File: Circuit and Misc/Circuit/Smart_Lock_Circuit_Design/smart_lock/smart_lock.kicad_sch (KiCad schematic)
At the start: 23 parts

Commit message: schematic development
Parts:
- removed J?: Bluepill header1, symbol Connector:Conn_01x20_Female
- removed J?: Bluepill header2, symbol Connector:Conn_01x20_Female
- added BT?: Battery, symbol Device:Battery
- added J?: RTC, symbol Connector:Conn_01x04_Male
- added R?: R, symbol Device:R
- added U? (x3): LM2596, symbol LM2596_Module:LM2596
- added U?: Bluepill_LDO, symbol Bluepill_LDO:Bluepill_LDO
- added U?: 24LC16, symbol Memory_EEPROM:24LC16
- added U?: STM32F103C8Tx, Package_QFP:LQFP-48_7x7mm_P0.5mm, symbol MCU_ST_STM32F1:STM32F103C8Tx
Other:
- note added: "DEVICES USING I2C COMMUNICATION"
- note added: "DEVICES USING UART COMMUNICATION"
- note added: "DRIVER CIRCUIT FOR BUZZER"
- note added: "DRIVER CIRCUIT FOR LOCK"
- note added: "GPIO INPUT DEVICES"
- note added: "MICROCONTROLLER"
- note added: "POWER SECTION"
- moved on the sheet: BZ?, D?, J?, L?, Q?, R?, SW?, U?A, U?B, U?C

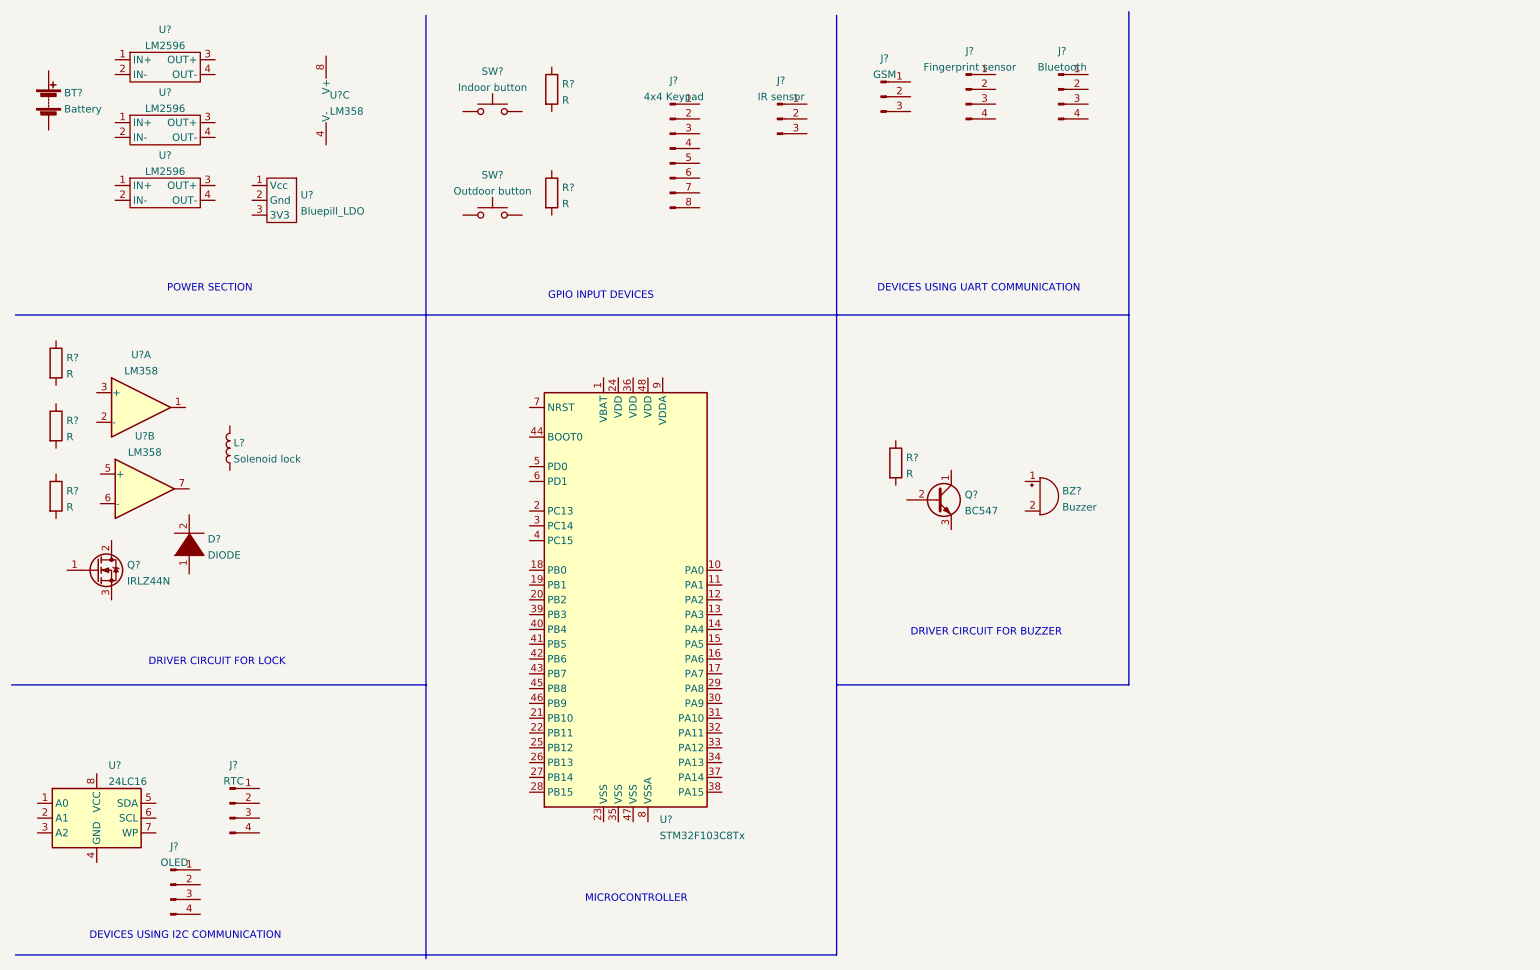
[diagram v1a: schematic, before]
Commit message: schematic update
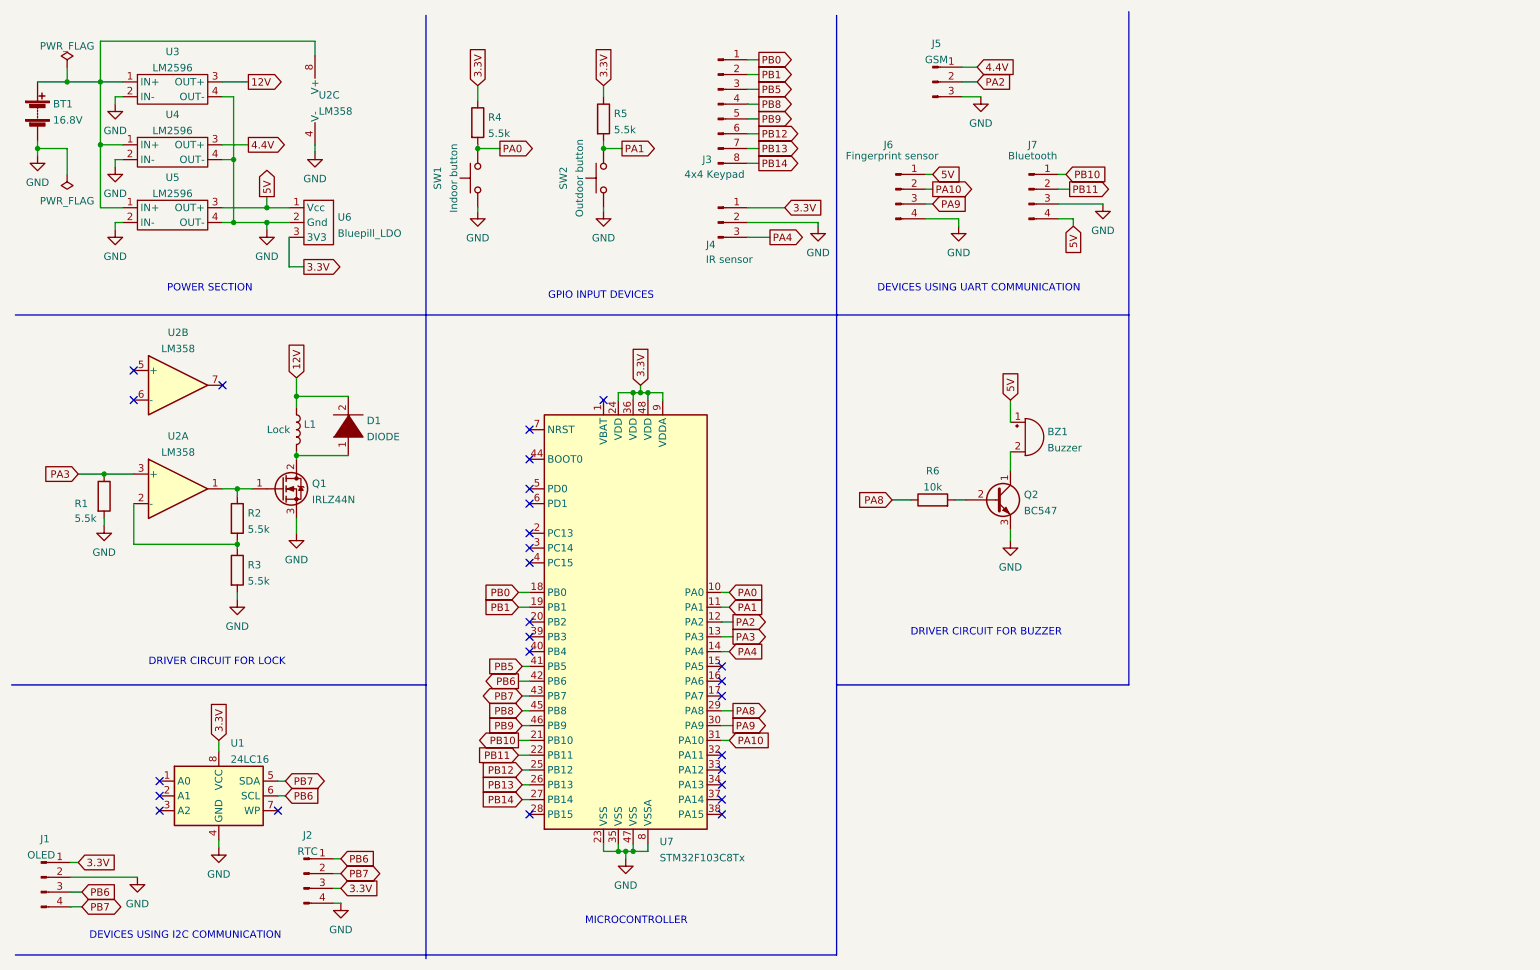
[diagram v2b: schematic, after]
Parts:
- removed U? (x3): LM2596, symbol LM2596_Module:LM2596
- added U3, U4, U5: LM2596, symbol LM2596_Module:LM2596
- BT1: renamed from BT?; value Battery -> 16.8V
- L1: renamed from L?; value Solenoid lock -> Lock
- R1, R2, R3, R4, R5: renamed from R?; value R -> 5.5k
- R6: renamed from R?; value R -> 10k
- gave numbers to parts that had none: 17
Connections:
- net 12V: now reaches L1.1
- net 12V: now also D1.2 (A), U3.3 (OUT+)
- net at L1.2: now also D1.1 (K), Q1.2 (D)
- net GND: now reaches SW1.1 (A), SW1.2 (A)
- net GND: now also BT1.2 (-), J1.2 (Pin_2), J2.4 (Pin_4), J4.2 (Pin_2), J5.3 (Pin_3), J6.4 (Pin_4), J7.3 (Pin_3), Q1.3 (S), Q2.3 (E), R1.2, R3.2, SW2.1 (A), SW2.2 (A), U1.4 (GND), U2.4 (V-), U6.2 (Gnd), U7.23 (VSS), U7.35 (VSS), U7.47 (VSS), U7.8 (VSSA), U3.2 (IN-), U3.4 (OUT-), U4.2 (IN-), U4.4 (OUT-), U5.2 (IN-), U5.4 (OUT-)
- net PA0: now reaches SW1.3 (B), SW1.4 (B)
- net PA0: now also R4.2, U7.10 (PA0)
- net PB6: now reaches J2.1 (Pin_1)
- net PB6: now also J1.3 (Pin_3), U1.6 (SCL), U7.42 (PB6)
- net PB7: now reaches J2.2 (Pin_2)
- net PB7: now also J1.4 (Pin_4), U1.5 (SDA), U7.43 (PB7)
- net 3.3V: now reaches J2.3 (Pin_3)
- net 3.3V: now also J1.1 (Pin_1), J4.1 (Pin_1), R4.1, R5.1, U1.8 (VCC), U6.3 (3V3), U7.24 (VDD), U7.36 (VDD), U7.48 (VDD), U7.9 (VDDA)
- net PB0: now reaches J3.1 (Pin_1)
- net PB0: now also U7.18 (PB0)
- net PB1: now reaches J3.2 (Pin_2)
- net PB1: now also U7.19 (PB1)
- net PB5: now reaches J3.3 (Pin_3)
- net PB5: now also U7.41 (PB5)
- net PB8: now reaches J3.4 (Pin_4)
- net PB8: now also U7.45 (PB8)
- net PB9: now reaches J3.5 (Pin_5)
- net PB9: now also U7.46 (PB9)
- net PB12: now reaches J3.6 (Pin_6)
- net PB12: now also U7.25 (PB12)
- net PB13: now reaches J3.7 (Pin_7)
- net PB13: now also U7.26 (PB13)
- net PB14: now reaches J3.8 (Pin_8)
- net PB14: now also U7.27 (PB14)
- net at U2.1: now also Q1.1 (G), R2.1
- net at U2.2 (-): now also R2.2, R3.1
- net PA3: now reaches U2.3 (+)
- net PA3: now also R1.1, U7.13 (PA3)
- net PA4: now reaches J4.3 (Pin_3)
- net PA4: now also U7.14 (PA4)
- net 5V: now reaches J6.1 (Pin_1)
- net 5V: now also BZ1.1 (-), J7.4 (Pin_4), U6.1 (Vcc), U5.3 (OUT+)
- net PA10: now reaches J6.2 (Pin_2)
- net PA10: now also U7.31 (PA10)
- net PA9: now reaches J6.3 (Pin_3)
- net PA9: now also U7.30 (PA9)
- net PB10: now reaches J7.1 (Pin_1)
- net PB10: now also U7.21 (PB10)
- net PB11: now reaches J7.2 (Pin_2)
- net PB11: now also U7.22 (PB11)
- net at BZ1.2 (+): now also Q2.1 (C)
- net PA8: now reaches R6.1
- net PA8: now also U7.29 (PA8)
- net at R6.2: now also Q2.2 (B)
- net PA1: now reaches SW2.3 (B), SW2.4 (B)
- net PA1: now also R5.2, U7.11 (PA1)
- net 4.4V: now reaches J5.1 (Pin_1)
- net 4.4V: now also U4.3 (OUT+)
- net PA2: now reaches J5.2 (Pin_2)
- net PA2: now also U7.12 (PA2)
- net at BT1.1 (+): now also U2.8 (V+), U3.1 (IN+), U4.1 (IN+), U5.1 (IN+)
- no-connect marks 0 -> 27
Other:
- moved on the sheet: BT1, BZ1, D1, J1, J2, J3, J4, J5, J6, J7, L1, Q1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

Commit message: updated schematic
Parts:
- removed J4: IR sensor, symbol Connector:Conn_01x03_Male
- added J4: Ultrasonic sensor, symbol Connector:Conn_01x04_Male
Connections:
- net 5V: now also J4.1 (Pin_1)
- net GND: now also J4.2 (Pin_2)
- net PA4: now also J4.3 (Pin_3)
- net PA6: now reaches U7.16 (PA6)
- net PA6: now also J4.4 (Pin_4)
- no-connect marks 27 -> 26
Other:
- note added: "Echo"
- note added: "Trig"
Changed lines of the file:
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@@
   (no_connect (at 100.33 118.745))
   (no_connect (at 133.35 128.905))
-  (no_connect (at 133.35 126.365))
   (no_connect (at 133.35 123.825))
   (no_connect (at 100.33 116.205))
@@
     (stroke (width 0) (type default) (color 0 0 0 0))
   )
-  (wire (pts (xy 137.795 45.085) (xy 144.145 45.085))
+  (wire (pts (xy 134.62 49.53) (xy 137.795 49.53))
+    (stroke (width 0) (type default) (color 0 0 0 0))
+  )
+  (wire (pts (xy 134.62 52.07) (xy 149.225 52.07))
     (stroke (width 0) (type default) (color 0 0 0 0))
   )
@@
     (stroke (width 0) (type default) (color 0 0 0 0))
   )
+  (wire (pts (xy 134.62 57.15) (xy 137.795 57.15))
+    (stroke (width 0) (type default) (color 0 0 0 0))
+  )
   (wire (pts (xy 21.59 162.56) (xy 23.495 162.56))
     (stroke (width 0) (type default) (color 0 0 0 0))
@@
     (stroke (width 0) (type default) (color 0 0 0 0))
   )
-  (wire (pts (xy 137.795 47.625) (xy 149.86 47.625))
-    (stroke (width 0) (type default) (color 0 0 0 0))
-  )
   (wire (pts (xy 29.21 47.625) (xy 30.48 47.625))
     (stroke (width 0) (type default) (color 0 0 0 0))
@@
     (stroke (width 0) (type default) (color 0 0 0 0))
   )
-  (wire (pts (xy 149.86 47.625) (xy 149.86 48.26))
+  (wire (pts (xy 149.225 52.07) (xy 149.225 52.705))
     (stroke (width 0) (type default) (color 0 0 0 0))
   )
@@
     (stroke (width 0) (type default) (color 0 0 0 0))
   )
-  (wire (pts (xy 137.795 50.165) (xy 141.605 50.165))
+  (wire (pts (xy 134.62 54.61) (xy 137.16 54.61))
     (stroke (width 0) (type default) (color 0 0 0 0))
   )
@@
     (stroke (width 0) (type default) (color 0 0 0 0))
   )
+  (wire (pts (xy 133.35 126.365) (xy 135.255 126.365))
+    (stroke (width 0) (type default) (color 0 0 0 0))
+  )
   (wire (pts (xy 98.425 139.065) (xy 100.33 139.065))
     (stroke (width 0) (type default) (color 0 0 0 0))
@@
     (stroke (width 0) (type default) (color 0 0 0 0))
   )
-  (wire (pts (xy 133.35 121.285) (xy 134.62 121.285))
+  (wire (pts (xy 133.35 121.285) (xy 135.255 121.285))
     (stroke (width 0) (type default) (color 0 0 0 0))
   )
@@
     (stroke (width 0) (type default) (color 0 0 0 0))
   )
-  (text "GPIO INPUT DEVICES" (at 103.505 60.96 0)
+  (text "Echo" (at 124.46 57.785 0)
     (effects (font (size 1.27 1.27)) (justify left bottom))
   )
-  (text "DEVICES USING UART COMMUNICATION" (at 160.02 59.69 0)
+  (text "GPIO INPUT DEVICES" (at 106.68 62.865 0)
     (effects (font (size 1.27 1.27)) (justify left bottom))
   )
-  (text "DEVICES USING I2C COMMUNICATION" (at 24.765 170.815 0)
+  (text "DEVICES USING UART COMMUNICATION" (at 161.925 62.865 0)
     (effects (font (size 1.27 1.27)) (justify left bottom))
   )
-  (text "DRIVER CIRCUIT FOR BUZZER" (at 165.735 118.745 0)
+  (text "DEVICES USING I2C COMMUNICATION" (at 27.94 172.72 0)
     (effects (font (size 1.27 1.27)) (justify left bottom))
   )
-  (text "DRIVER CIRCUIT FOR LOCK" (at 34.925 123.825 0)
+  (text "Trig" (at 125.73 55.245 0)
     (effects (font (size 1.27 1.27)) (justify left bottom))
   )
-  (text "MICROCONTROLLER" (at 109.855 168.275 0)
+  (text "DRIVER CIRCUIT FOR BUZZER" (at 168.275 126.365 0)
     (effects (font (size 1.27 1.27)) (justify left bottom))
   )
-  (text "POWER SECTION" (at 38.1 59.69 0)
+  (text "DRIVER CIRCUIT FOR LOCK" (at 36.195 126.365 0)
+    (effects (font (size 1.27 1.27)) (justify left bottom))
+  )
+  (text "MICROCONTROLLER" (at 111.125 172.72 0)
+    (effects (font (size 1.27 1.27)) (justify left bottom))
+  )
+  (text "POWER SECTION" (at 38.1 62.865 0)
     (effects (font (size 1.27 1.27)) (justify left bottom))
   )
@@
     )
   )
-  (global_label "PA4" (shape input) (at 134.62 121.285 0) (fields_autoplaced)
-    (effects (font (size 1.27 1.27)) (justify left))
-    (property "Intersheet References" "${INTERSHEET_REFS}" (id 0) (at 140.6012 121.2056 0)
+  (global_label "PA6" (shape input) (at 135.255 126.365 0) (fields_autoplaced)
+    (effects (font (size 1.27 1.27)) (justify left))
+    (property "Intersheet References" "${INTERSHEET_REFS}" (id 0) (at 141.2362 126.2856 0)
+      (effects (font (size 1.27 1.27)) (justify left) hide)
+    )
+  )
+  (global_label "PA4" (shape output) (at 135.255 121.285 0) (fields_autoplaced)
+    (effects (font (size 1.27 1.27)) (justify left))
+    (property "Intersheet References" "${INTERSHEET_REFS}" (id 0) (at 141.2362 121.2056 0)
       (effects (font (size 1.27 1.27)) (justify left) hide)
     )
@@
     (effects (font (size 1.27 1.27)) (justify left))
     (property "Intersheet References" "${INTERSHEET_REFS}" (id 0) (at 145.8626 19.6056 0)
+      (effects (font (size 1.27 1.27)) (justify left) hide)
+    )
+  )
+  (global_label "PA6" (shape output) (at 137.795 57.15 0) (fields_autoplaced)
+    (effects (font (size 1.27 1.27)) (justify left))
+    (property "Intersheet References" "${INTERSHEET_REFS}" (id 0) (at 143.7762 57.0706 0)
       (effects (font (size 1.27 1.27)) (justify left) hide)
     )
@@
     )
   )
-  (global_label "PA4" (shape output) (at 141.605 50.165 0) (fields_autoplaced)
-    (effects (font (size 1.27 1.27)) (justify left))
-    (property "Intersheet References" "${INTERSHEET_REFS}" (id 0) (at 147.5862 50.0856 0)
+  (global_label "PA4" (shape input) (at 137.16 54.61 0) (fields_autoplaced)
+    (effects (font (size 1.27 1.27)) (justify left))
+    (property "Intersheet References" "${INTERSHEET_REFS}" (id 0) (at 143.1412 54.5306 0)
       (effects (font (size 1.27 1.27)) (justify left) hide)
     )
@@
     )
   )
-  (global_label "3.3V" (shape input) (at 144.145 45.085 0) (fields_autoplaced)
-    (effects (font (size 1.27 1.27)) (justify left))
-    (property "Intersheet References" "${INTERSHEET_REFS}" (id 0) (at 150.6705 45.0056 0)
+  (global_label "5V" (shape input) (at 137.795 49.53 0) (fields_autoplaced)
+    (effects (font (size 1.27 1.27)) (justify left))
+    (property "Intersheet References" "${INTERSHEET_REFS}" (id 0) (at 142.5062 49.4506 0)
       (effects (font (size 1.27 1.27)) (justify left) hide)
     )
@@
     (pin "1")
   )
-  (symbol (lib_id "Connector:Conn_01x03_Male") (at 132.715 47.625 0) (unit 1)
-    (in_bom yes) (on_board yes)
-    (property "Reference" "J4" (id 0) (at 131.445 51.435 0))
-    (property "Value" "IR sensor" (id 1) (at 134.62 53.975 0))
-    (property "Footprint" "" (id 2) (at 132.715 47.625 0)
-      (effects (font (size 1.27 1.27)) hide)
-    )
-    (property "Datasheet" "~" (id 3) (at 132.715 47.625 0)
-      (effects (font (size 1.27 1.27)) hide)
-    )
-    (pin "1")
-    (pin "2")
-    (pin "3")
-  )
   (symbol (lib_id "Connector:Conn_01x04_Male") (at 163.195 41.91 0) (unit 1)
     (in_bom yes) (on_board yes)
@@
     (pin "4")
   )
-  (symbol (lib_id "power:GND") (at 149.86 48.26 0) (unit 1)
-    (in_bom yes) (on_board yes) (fields_autoplaced)
-    (property "Reference" "#PWR011" (id 0) (at 149.86 54.61 0)
-      (effects (font (size 1.27 1.27)) hide)
-    )
-    (property "Value" "GND" (id 1) (at 149.86 52.8225 0))
-    (property "Footprint" "" (id 2) (at 149.86 48.26 0)
-      (effects (font (size 1.27 1.27)) hide)
-    )
-    (property "Datasheet" "" (id 3) (at 149.86 48.26 0)
+  (symbol (lib_id "power:GND") (at 149.225 52.705 0) (unit 1)
+    (in_bom yes) (on_board yes) (fields_autoplaced)
+    (property "Reference" "#PWR011" (id 0) (at 149.225 59.055 0)
+      (effects (font (size 1.27 1.27)) hide)
+    )
+    (property "Value" "GND" (id 1) (at 149.225 57.2675 0))
+    (property "Footprint" "" (id 2) (at 149.225 52.705 0)
+      (effects (font (size 1.27 1.27)) hide)
+    )
+    (property "Datasheet" "" (id 3) (at 149.225 52.705 0)
       (effects (font (size 1.27 1.27)) hide)
     )
@@
     (pin "2")
     (pin "3")
+  )
+  (symbol (lib_id "Connector:Conn_01x04_Male") (at 129.54 52.07 0) (unit 1)
+    (in_bom yes) (on_board yes)
+    (property "Reference" "J4" (id 0) (at 128.27 44.45 0))
+    (property "Value" "Ultrasonic sensor" (id 1) (at 128.905 46.355 0))
+    (property "Footprint" "" (id 2) (at 129.54 52.07 0)
+      (effects (font (size 1.27 1.27)) hide)
+    )
+    (property "Datasheet" "~" (id 3) (at 129.54 52.07 0)
+      (effects (font (size 1.27 1.27)) hide)
+    )
+    (pin "1")
+    (pin "2")
+    (pin "3")
+    (pin "4")
   )
   (symbol (lib_id "Device:R") (at 113.03 29.845 0) (unit 1)
@@
       (reference "J3") (unit 1) (value "4x4 Keypad") (footprint "")
     )
-    (path "/63479272-0704-44b9-a883-ef4995c1df4e"
-      (reference "J4") (unit 1) (value "IR sensor") (footprint "")
+    (path "/bc6effc8-87db-4893-b9a4-0083d7cf18d2"
+      (reference "J4") (unit 1) (value "Ultrasonic sensor") (footprint "")
     )
     (path "/ba332a8c-8cb0-4198-9add-89840c85b387"

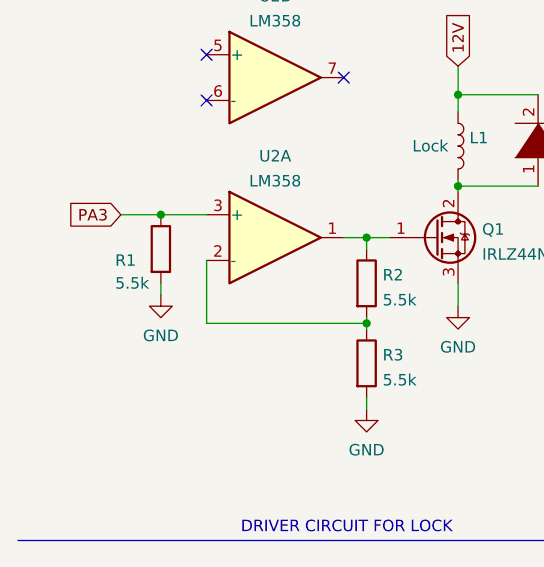
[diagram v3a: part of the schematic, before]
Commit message: schematic update
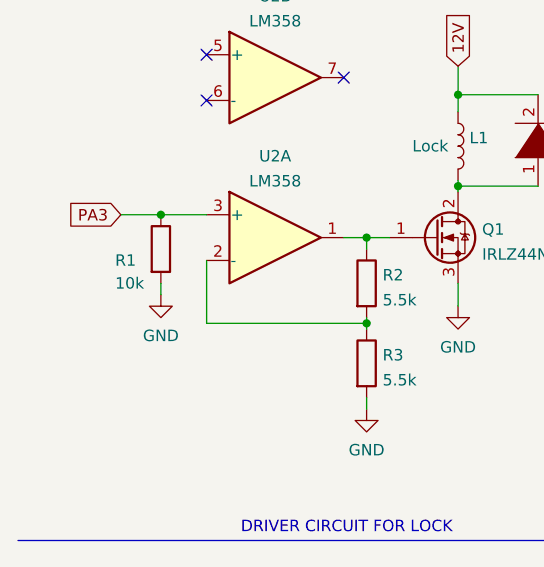
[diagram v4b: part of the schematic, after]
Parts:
- R1: value 5.5k -> 10k
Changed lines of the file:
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@@
       (effects (font (size 1.27 1.27)) (justify left))
     )
-    (property "Value" "5.5k" (id 1) (at 22.225 98.425 0)
+    (property "Value" "10k" (id 1) (at 22.225 98.425 0)
       (effects (font (size 1.27 1.27)) (justify left))
     )
@@
     )
     (path "/5591601a-0208-417f-b6e4-bd68e0c1316e"
-      (reference "R1") (unit 1) (value "5.5k") (footprint "")
+      (reference "R1") (unit 1) (value "10k") (footprint "")
     )
     (path "/91b64d2e-f7fe-475a-ae8e-f382e512b883"

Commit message: update
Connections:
- net 3.3V: now also J6.1 (Pin_1)
- net 5V: no longer J6.1 (Pin_1)
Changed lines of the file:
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@@
     )
   )
-  (global_label "5V" (shape input) (at 169.545 39.37 0) (fields_autoplaced)
+  (global_label "3.3V" (shape input) (at 169.545 39.37 0) (fields_autoplaced)
     (effects (font (size 1.27 1.27)) (justify left))
-    (property "Intersheet References" "${INTERSHEET_REFS}" (id 0) (at 174.2562 39.2906 0)
+    (property "Intersheet References" "${INTERSHEET_REFS}" (id 0) (at 176.0705 39.2906 0)
       (effects (font (size 1.27 1.27)) (justify left) hide)
     )
